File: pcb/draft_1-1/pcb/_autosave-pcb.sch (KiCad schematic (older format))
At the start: 23 parts, among them J1 USB4110-GF-A, U1 H3LIS200DLTR, U2 ATSAML21J16B-AUT, U3 BQ25155

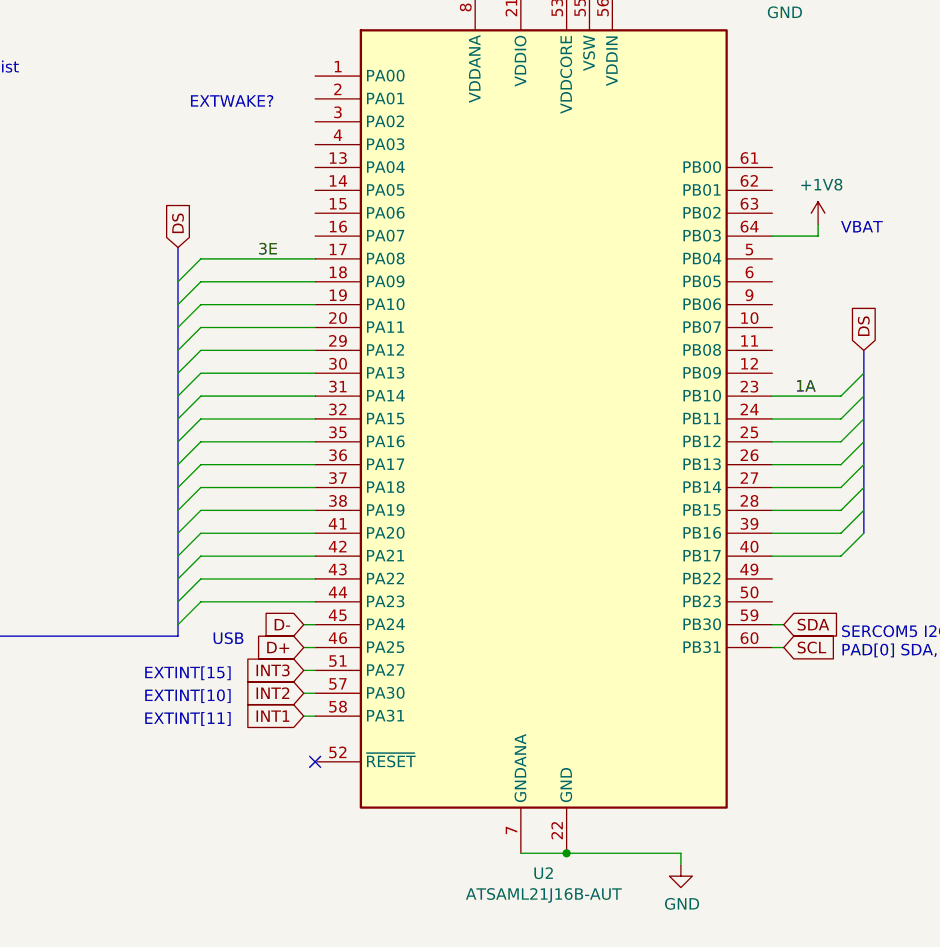
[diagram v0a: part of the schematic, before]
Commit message: PRE-TRACE PLACEMENT CHECKPOINT
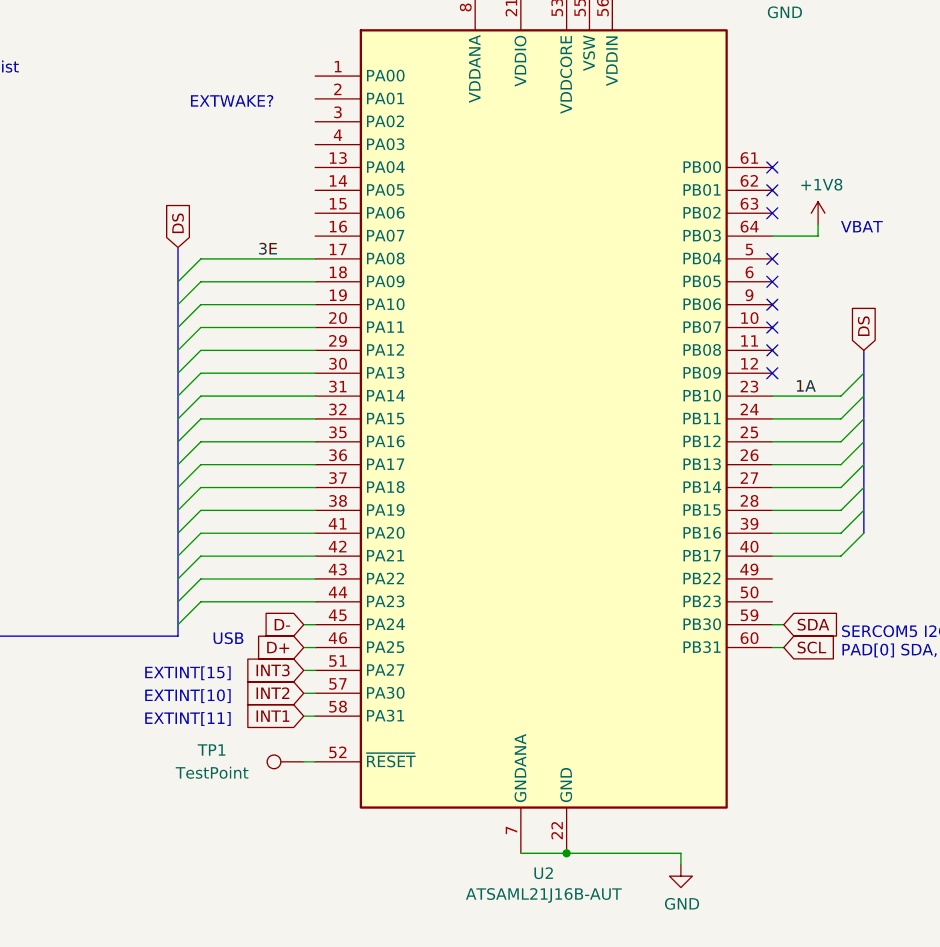
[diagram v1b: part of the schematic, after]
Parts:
- added TP1: TestPoint, TestPoint:TestPoint_Pad_1.0x1.0mm, symbol Connector:TestPoint
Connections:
- net at U2.52 (~RESET): now also TP1.1
- no-connect marks 9 -> 17
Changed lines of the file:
@@
 Wire Wire Line
 	8500 1300 9100 1300
-NoConn ~ 7800 5500
 Wire Wire Line
 	9100 1300 9100 2100
@@
 SCL
 Wire Wire Line
-	8700 5900 8900 5900
-$Comp
-L MCU_Microchip_SAML:ATSAML21J16B-AUT U2
-U 1 1 5E306B11
-P 8800 4000
-F 0 "U2" H 8800 2011 50  0000 C CNN
-F 1 "ATSAML21J16B-AUT" H 8800 1920 50  0000 C CNN
-F 2 "Package_QFP:TQFP-64_10x10mm_P0.5mm" H 10000 5800 50  0001 C CNN
-F 3 "http://ww1.microchip.com/downloads/en/DeviceDoc/60001477A.pdf" H 8800 4000 50  0001 C CNN
-	1    8800 4000
-	1    0    0    -1
-$EndComp
-Wire Wire Line
-	8900 5900 9400 5900
-Connection ~ 8900 5900
-Wire Wire Line
 	9400 5950 9400 5900
 Wire Wire Line
@@
 VBAT
 NoConn ~ 4200 2850
+NoConn ~ 9800 2900
+NoConn ~ 9800 3000
+NoConn ~ 9800 3100
+NoConn ~ 9800 3300
+NoConn ~ 9800 3400
+NoConn ~ 9800 3500
+NoConn ~ 9800 3600
+NoConn ~ 9800 3700
+NoConn ~ 9800 3800
+Wire Wire Line
+	8900 5900 9400 5900
+Wire Wire Line
+	8700 5900 8900 5900
+Connection ~ 8900 5900
+$Comp
+L MCU_Microchip_SAML:ATSAML21J16B-AUT U2
+U 1 1 5E306B11
+P 8800 4000
+F 0 "U2" H 8800 2011 50  0000 C CNN
+F 1 "ATSAML21J16B-AUT" H 8800 1920 50  0000 C CNN
+F 2 "Package_QFP:TQFP-64_10x10mm_P0.5mm" H 10000 5800 50  0001 C CNN
+F 3 "http://ww1.microchip.com/downloads/en/DeviceDoc/60001477A.pdf" H 8800 4000 50  0001 C CNN
+	1    8800 4000
+	1    0    0    -1
+$EndComp
+$Comp
+L Connector:TestPoint TP1
+U 1 1 5E430727
+P 7750 5500
+F 0 "TP1" V 7800 5900 50  0000 C CNN
+F 1 "TestPoint" V 7700 5900 50  0000 C CNN
+F 2 "TestPoint:TestPoint_Pad_1.0x1.0mm" H 7950 5500 50  0001 C CNN
+F 3 "~" H 7950 5500 50  0001 C CNN
+	1    7750 5500
+	0    -1   -1   0
+$EndComp
+Wire Wire Line
+	7750 5500 7800 5500
 Wire Bus Line
 	10200 3700 10200 4500
